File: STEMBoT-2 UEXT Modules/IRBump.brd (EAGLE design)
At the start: 21.6 x 26.3 mm, 21 parts, among them IC1 LMV324DR2G, IC2 LMV324DR2G, IC3 74HC165PW,118, Q1 MMBT3904LP-7

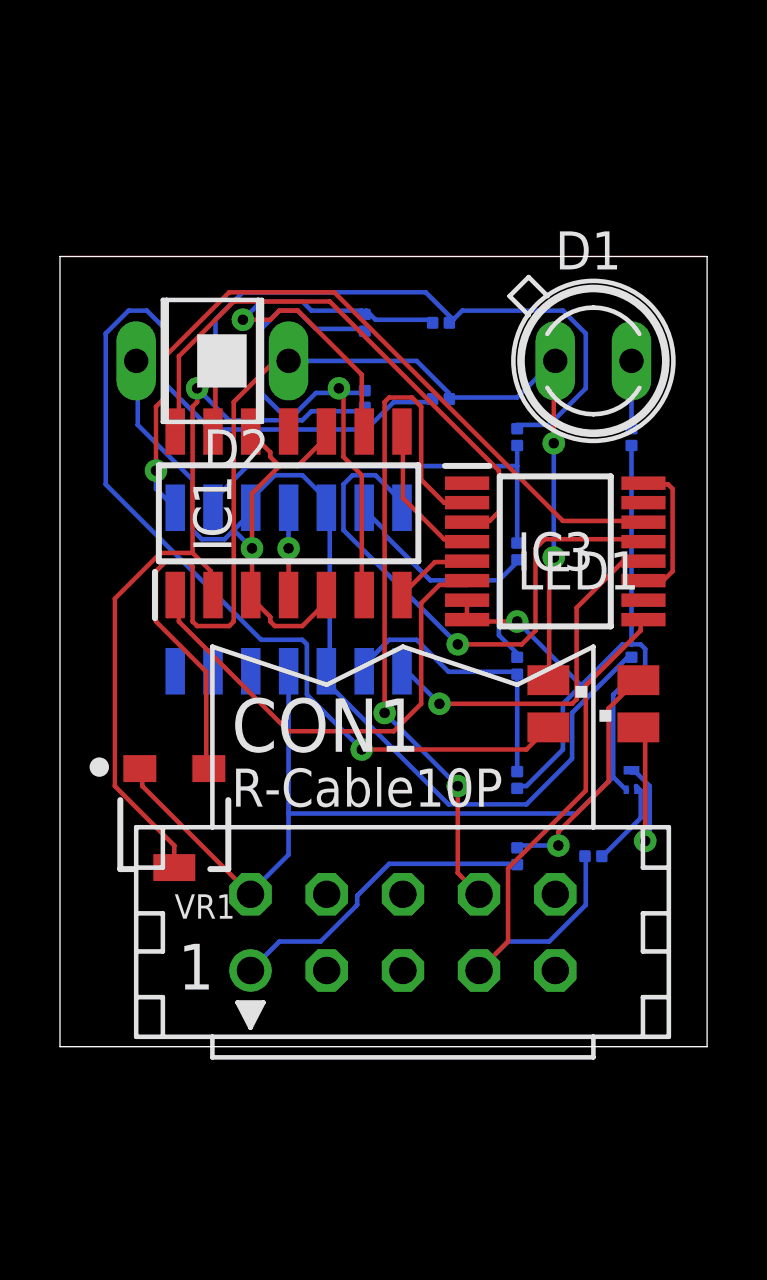
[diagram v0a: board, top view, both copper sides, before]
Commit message: Adjusted ADC modules for PCB order. Dan, these are auto-routed.
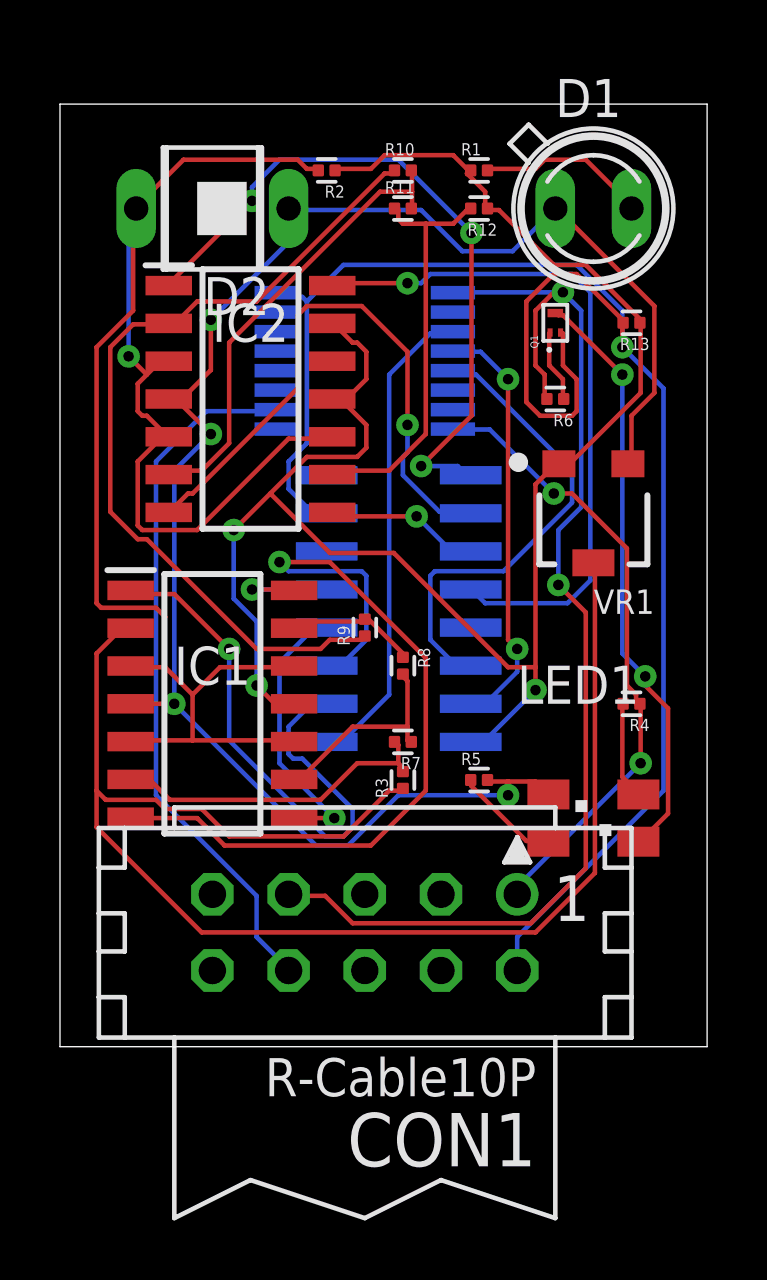
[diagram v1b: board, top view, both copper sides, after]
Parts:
- added R13: ERJ-1RHD3601C, Resistor:RESC0603X26N
- added U1: SN74HC148D, SN74HC148D:SOIC127P600X175-16N
- moved R2 19.4 mm to (8.89, 29.2), flipped to the top, turned to 180 degrees
- moved R12 19.1 mm to (14.0, 27.9), flipped to the top, turned to 180 degrees
- moved VR1 17.3 mm to (17.8, 17.8)
- moved R11 15.7 mm to (11.4, 27.9), flipped to the top, turned to 0 degrees
- moved Q1 15.5 mm to (16.5, 24.1), flipped to the top
- moved R6 15.3 mm to (16.5, 21.6), flipped to the top, turned to 180 degrees
- moved R7 14.0 mm to (11.4, 10.2), flipped to the top, turned to 180 degrees
- moved R10 13.3 mm to (11.4, 29.2), flipped to the top, turned to 0 degrees
- moved R3 12.8 mm to (11.4, 8.89), flipped to the top
- moved R5 12.8 mm to (14.0, 8.89), flipped to the top, turned to 0 degrees
- moved R8 11.5 mm to (11.4, 12.7), flipped to the top, turned to 270 degrees
- moved R1 10.2 mm to (14.0, 29.2), flipped to the top, turned to 0 degrees
- moved IC3 8.98 mm to (10.2, 22.9), flipped to the bottom, turned to 180 degrees
- moved R9 8.13 mm to (10.2, 14.0), flipped to the top
- moved IC1 6.84 mm to (5.08, 11.4), turned to 0 degrees
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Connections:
- removed net N$26 (its old number): IC3.11, IC3.16
- removed net V+: IC1.4, IC2.4
- removed net V-: IC1.11
- new net N$21: IC1.11, IC2.11, IC2.13, R1.1, R12.1, R13.1, R2.1, U1.8, VR1.1
- new net N$28: IC3.11, U1.9
- new net N$29: IC3.12, U1.7
- new net N$30: IC3.13, U1.6
- new net N$4: CON1.2, IC3.8, Q1.2, R13.2, U1.15
- new net VCC: U1.16
- net N$1: now also IC2.8, U1.3; no longer CON1.2, IC2.11, IC3.7, IC3.8, Q1.2, R1.1, R12.1, R2.1, VR1.1
- net N$11: now also U1.1; no longer IC3.14
- net N$13: now also U1.2; no longer IC3.13
- net N$17: now also IC3.16
- net N$22: now also U1.13; no longer IC3.3
- net N$23: now also U1.12; no longer IC3.4
- net N$24: now also U1.11; no longer IC3.5
- net N$25: now also U1.10; no longer IC3.6
- net N$6: now also IC1.4, IC2.4
- net N$9: now also IC2.14, U1.4; no longer IC2.8, IC3.12
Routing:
- net N$21: track 0.00 -> 60.2 mm, vias 0 -> 3
- net N$4: track 0.00 -> 58.8 mm, vias 0 -> 1
- net N$1: track 49.8 -> 5.17 mm
- net N$3: track 39.1 -> 3.53 mm, vias 1 -> 0
- net N$24: track 2.65 -> 28.5 mm, vias 0 -> 1
- net N$14: track 26.5 -> 48.1 mm, vias 1 -> 0
- net N$31: track 20.1 -> 39.2 mm, vias 0 -> 2
- net N$18: track 22.2 -> 4.40 mm, vias 1 -> 0
- net N$28: track 0.00 -> 16.1 mm
- net N$30: track 0.00 -> 16.1 mm
- net N$6: track 42.6 -> 58.0 mm, vias 2 -> 4
- net N$22: track 18.9 -> 3.91 mm, vias 0 -> 1
- net N$29: track 0.00 -> 14.1 mm, vias 0 -> 2
- net N$19: track 14.1 -> 28.0 mm
- net N$8: track 6.63 -> 19.7 mm, vias 1 -> 2
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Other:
- board size 21.6 x 26.3 mm -> 21.6 x 31.4 mm

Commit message: Once again, updating ADC shematics and boards. Used autorouter.
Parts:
- removed IC1, IC2: LMV324DR2G, LMV324DR2G:SOP126P600X175-14N
- added R14, R15: ERJ-1RHD3601C, Resistor:RESC0603X26N
- added U2, U3: MAX964ESET, MAX964ESET:SOIC127P600X175-16N
- moved R13 18.9 mm to (1.27, 17.8), turned to 90 degrees
- moved R10 18.2 mm to (15.2, 11.4), flipped to the bottom, turned to 270 degrees
- moved U1 17.3 mm to (19.1, 24.1), turned to 180 degrees
- moved R12 16.9 mm to (10.2, 11.4), flipped to the bottom, turned to 270 degrees
- moved R11 14.5 mm to (15.2, 14.0), flipped to the bottom
- moved R6 13.7 mm to (11.4, 8.89), flipped to the bottom, turned to 270 degrees
- moved R3 12.7 mm to (11.4, 21.6), flipped to the bottom, turned to 180 degrees
- moved VR1 12.5 mm to (6.35, 22.9), turned to 270 degrees
- moved R9 8.89 mm to (1.27, 14.0)
- moved R4 6.35 mm to (19.1, 5.08), flipped to the bottom
- moved R7 5.39 mm to (7.62, 14.0), flipped to the bottom, turned to 90 degrees
- moved Q1 5.08 mm to (11.4, 24.1), turned to 0 degrees
- moved IC3 3.81 mm to (6.35, 22.9)
- moved R8 2.84 mm to (10.2, 15.2), flipped to the bottom
- moved R1 1.80 mm to (12.7, 27.9)
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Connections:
- removed net N$21: IC1.11, IC2.11, IC2.13, R1.1, R12.1, R13.1, R2.1, U1.8, VR1.1
- removed net VCC: U1.16
- new net N$27: U1.12, U3.14
- new net N$32: U1.11, U3.11
- new net N$33: U1.10, U3.10
- net N$1: now also R3.2, U2.2, U2.4, U2.6, U2.8, U3.2, U3.4, U3.6, U3.8; no longer IC2.8, U1.3
- net N$11: now also R10.2, R8.1, U2.3; no longer IC2.1, U1.1
- net N$13: now also R12.1, R8.2, U2.5; no longer IC2.7, U1.2
- net N$14: no longer IC1.2
- net N$15: now also R12.2, R7.1, U2.7; no longer IC1.6, R3.2, R7.2
- net N$16: now also R13.2, R7.2, U3.1; no longer IC1.9, R7.1, R8.2
- net N$18: now also R13.1, U3.3; no longer IC1.13, R8.1
- net N$19: now also R14.2, U3.5; no longer IC2.2, R10.1
- net N$20: now also R14.1, R15.2, U3.7; no longer IC2.6, R10.2, R11.2
- net N$22: now also U1.3, U2.14; no longer IC1.14, U1.13
- net N$23: now also U1.2, U2.11; no longer IC1.8, U1.12
- net N$24: now also U1.13, U2.10; no longer IC1.7, U1.11
- net N$25: now also U1.1, U3.15; no longer IC1.1, U1.10
- net N$4: now also R1.1, R15.1, R2.1, U1.8, U2.12, U3.12, VR1.1; no longer R13.2, U1.15
- net N$5: now also U1.4, U2.15; no longer IC2.9, R11.1, R12.2
- net N$6: now also R11.1, U1.16, U2.13, U3.13; no longer IC1.4, IC2.4
- net N$7: no longer IC1.10, IC1.12, IC1.3, IC1.5, IC2.10, IC2.3, IC2.5
- net N$9: now also R10.1, R11.2, U2.1; no longer IC2.14, U1.4
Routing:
- net N$21: track 60.2 -> 0.00 mm, vias 3 -> 0
- net N$1: track 5.17 -> 64.6 mm, vias 1 -> 4
- net N$7: track 58.8 -> 2.40 mm, vias 1 -> 0
- net N$14: track 48.1 -> 4.39 mm, vias 0 -> 1
- net N$33: track 0.00 -> 39.6 mm, vias 0 -> 3
- net N$32: track 0.00 -> 32.5 mm, vias 0 -> 1
- net N$27: track 0.00 -> 30.3 mm, vias 0 -> 3
- net N$19: track 28.0 -> 5.90 mm
- net N$12: track 2.42 -> 20.4 mm, vias 0 -> 1
- net N$4: track 58.8 -> 76.3 mm
- net N$31: track 39.2 -> 25.3 mm, vias 2 -> 0
- net N$13: track 19.8 -> 32.5 mm
- net N$15: track 10.8 -> 23.5 mm, vias 0 -> 1
- net N$11: track 23.4 -> 11.2 mm, vias 3 -> 2
- net N$25: track 18.7 -> 6.94 mm
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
